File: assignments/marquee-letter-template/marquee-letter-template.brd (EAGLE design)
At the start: 100 x 80 mm, 19 parts, among them Q2 MMBT2222A-TP

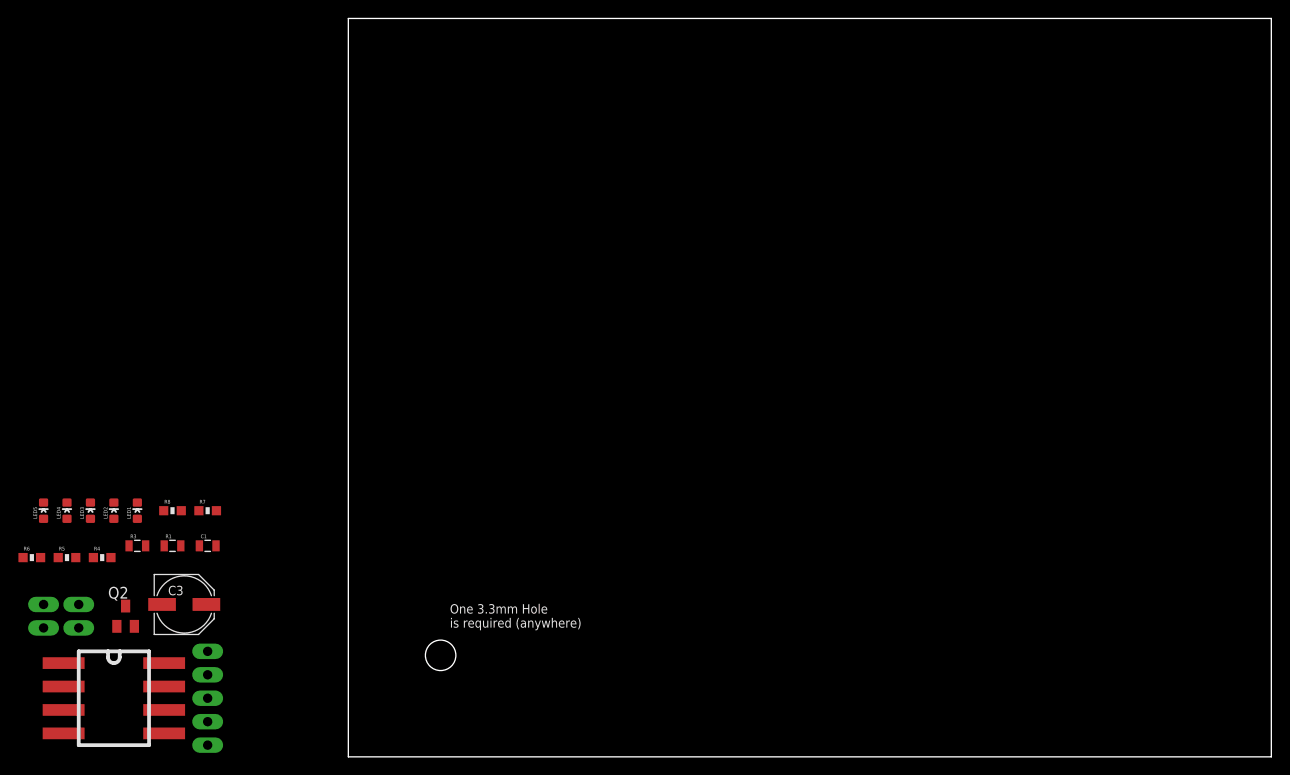
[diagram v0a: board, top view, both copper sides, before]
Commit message: marquee template; shrinks some footprints for marquee board
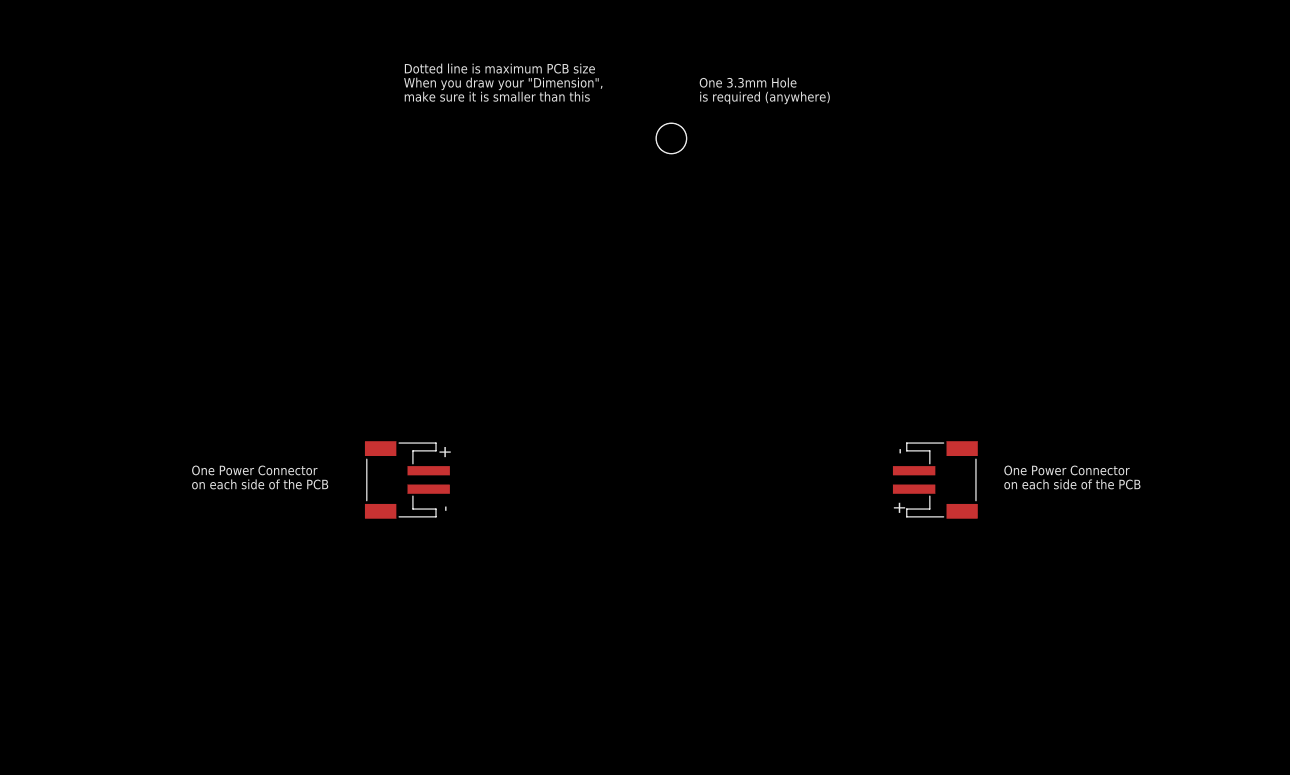
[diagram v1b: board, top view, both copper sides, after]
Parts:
- removed C1: 0.1uF, homemade-hardware:0805
- removed C3: 100uF, homemade-hardware:PANASONIC_D
- removed LED1, LED2, LED3, LED4, LED5: (no value), homemade-hardware:LED-0603
- removed POTENTIOMETER: HEADER-5, homemade-hardware:HEADER-5
- removed Q2: MMBT2222A-TP, homemade-hardware:SOT23
- removed R1: 10k, homemade-hardware:0805
- removed R3: 220, homemade-hardware:0805
- removed R4, R5, R6, R7, R8: 220, homemade-hardware:0603-RES
- removed U$3: HEADER-2, homemade-hardware:HEADER-2
- U$1: value ATTINY85-SOCKET-BENT -> CONN_BATTERY-LIPO-HORIZ; device homemade-hardware:SOCKET-8PIN-BENT -> homemade-hardware:JST-PH-2-SMT-RA
- U$2: value HEADER-2 -> CONN_BATTERY-LIPO-HORIZ; device homemade-hardware:HEADER-2 -> homemade-hardware:JST-PH-2-SMT-RA
- moved U$2 95.6 mm to (65.0, 30.0), turned to 270 degrees
- moved U$1 38.5 mm to (5.00, 30.0), turned to 90 degrees
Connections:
- removed net 5V: C1.1, C3.+, POTENTIOMETER.1, R1.2, R4.2, R5.2, R6.2, R7.2, R8.2, U$1.8, U$2.2, U$3.1
- removed net GND: C1.2, C3.-, POTENTIOMETER.5, Q2.2, U$1.4, U$2.1, U$3.2
- removed net N$1: LED1.A, R4.1
- removed net N$10: LED5.A, R8.1
- removed net N$12: R1.1, U$1.1
- removed net N$3: R3.2, U$1.5
- removed net N$4: LED1.C, LED2.C, LED3.C, LED4.C, LED5.C, Q2.3
- removed net N$5: Q2.1, R3.1
- removed net N$7: LED2.A, R5.1
- removed net N$8: LED3.A, R6.1
- removed net N$9: LED4.A, R7.1
- removed net SENSOR: POTENTIOMETER.3, U$1.3
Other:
- board outline removed
- board text added: "Dotted line is maximum PCB size When you draw your "Dimension", make sure it is smaller than this"
- board text added: "One Power Connector on each side of the PCB"
